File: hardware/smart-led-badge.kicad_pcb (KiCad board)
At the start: 4 copper layers, 118 x 76 mm, 1236 parts, among them J301 TYPE-C-31-M-12, J302 Battery JST-PH 2P, J501 SWD 2x5 1.27mm, Q201 AO3401A, Q202 AO3400A, Q203 AO3401A, Q204 AO3400A, Q301 AO3400A, Q302 AO3400A, Q303 AO3400A, Q701 AO3401A, Q702 AO3401A, Q703 AO3401A, Q704 AO3401A, Q705 AO3401A, Q706 AO3401A, Q707 AO3401A, Q708 AO3401A, Q709 AO3401A, Q710 AO3401A, Q711 AO3401A, Q712 AO3401A, Q713 AO3401A, Q714 AO3401A, Q715 AO3401A, Q716 AO3401A, Q717 AO3401A, Q718 AO3401A, Q719 AO3401A, Q720 AO3401A, Q721 AO3401A, Q722 AO3401A, Q723 AO3401A, Q724 AO3401A, Q725 AO3401A, Q726 AO3401A, Q727 AO3401A, Q728 AO3401A, Q729 AO3401A, Q730 AO3401A, Q731 AO3401A, Q732 AO3401A, SW1201 Mode/Next, SW1202 Action/Select, SW201 PCM12SMTR, U1101 NT3H2111W0FHKH, U201 TPS63802, U202 TPS61023, U301 TPD4E05U06, U302 BQ25620, U401 E73-2G4M08S1C, U601 TLC59283, U602 TLC59283, U701 SN74LVC8T245, U702 SN74HC595, U703 SN74HC595, U704 SN74HC595, U705 SN74HC595, U706 SN74LVC1G123, U707 SN74LVC1G04, U708 SN74LVC1G32, U901 ICM-42688-P, Y401 32.768kHz 9pF

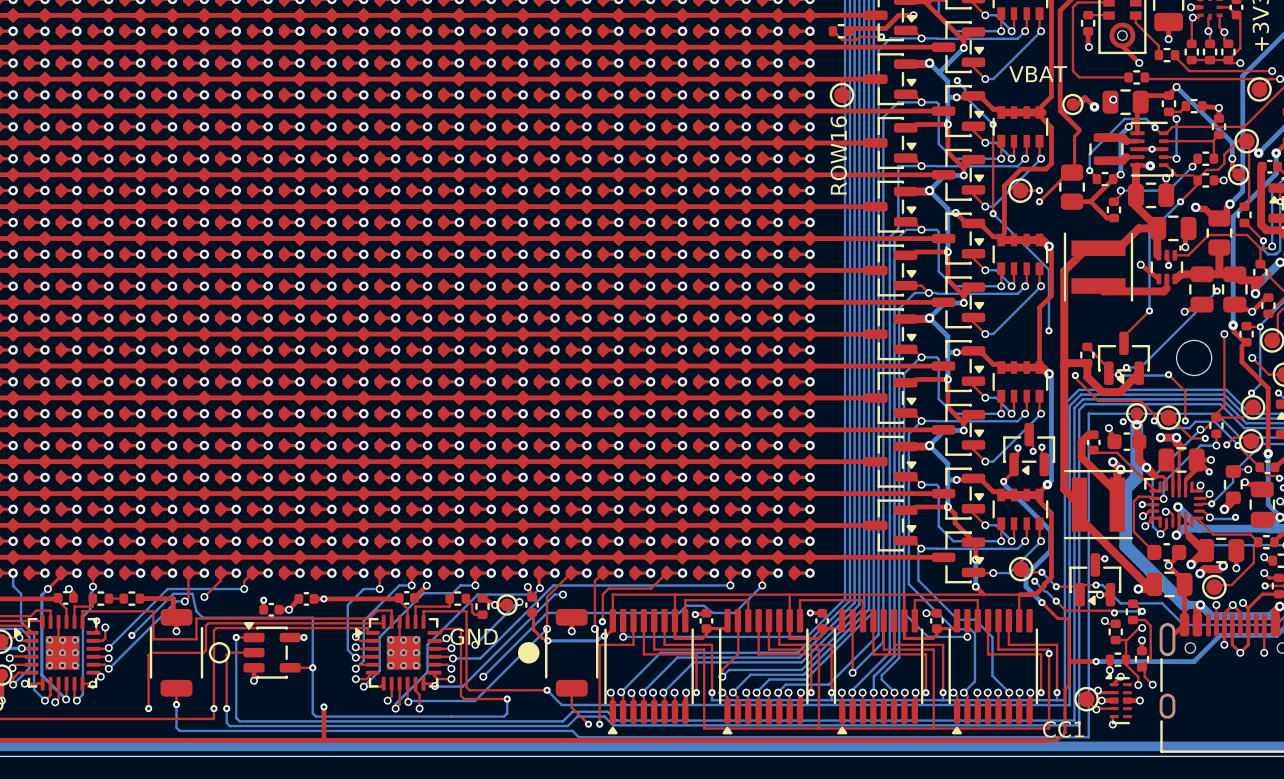
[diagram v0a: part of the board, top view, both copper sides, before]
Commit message: hw: move three vias out of component pads
The drill holes of the vias at C202.2, U201.8 and U601.13 reached into
the pads. Solder can wick down an open hole during reflow and starve the
joint, most of all on the two 0.25 mm-wide IC pins. Move the vias clear
of the pads, shifting the MODE_3V3 via and an In2 SYS segment to make
room, and refill the In1 GND plane.
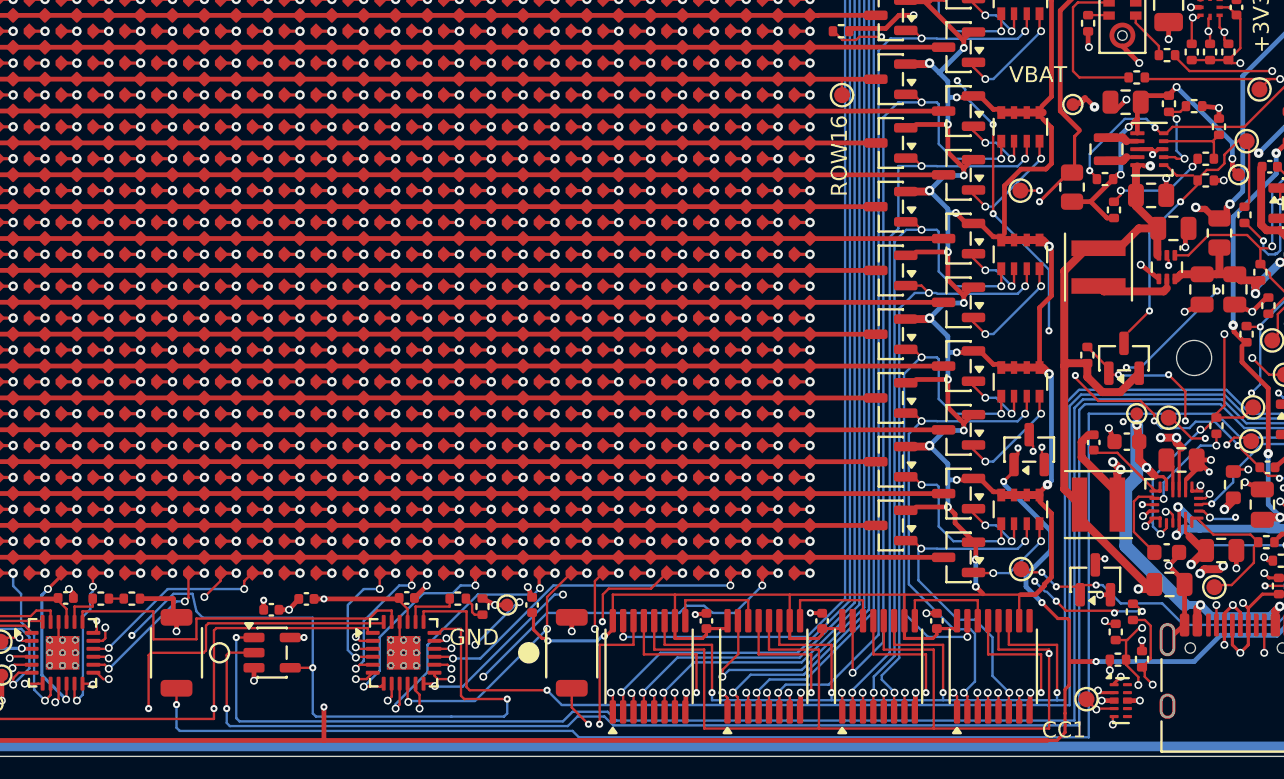
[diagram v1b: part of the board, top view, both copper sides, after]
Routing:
- net COL11: track 104.9 -> 106.0 mm
- net GND: track 108.8 -> 109.7 mm
- net /Regulators and Power Tree/MODE_3V3: track 5.19 -> 5.90 mm
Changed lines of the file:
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@@
 	)
 	(segment
+		(start 136.992185 88.239077)
+		(end 136.992185 87.952185)
+		(width 0.25)
+		(layer "F.Cu")
+		(net "GND")
+	)
+	(segment
 		(start 139 115.21)
 		(end 139 117.755)
@@
 	)
 	(segment
+		(start 136.94 87.9)
+		(end 136.24 87.9)
+		(width 0.25)
+		(layer "F.Cu")
+		(net "GND")
+	)
+	(segment
 		(start 134.5825 122.5)
 		(end 133.8 122.5)
@@
 	)
 	(segment
+		(start 134.679999 85.46)
+		(end 135.35 84.789999)
+		(width 0.3)
+		(layer "F.Cu")
+		(net "GND")
+	)
+	(segment
 		(start 143.88 109.25)
 		(end 142.785448 108.796621)
@@
 	)
 	(segment
+		(start 134.529999 85.46)
+		(end 134.679999 85.46)
+		(width 0.3)
+		(layer "F.Cu")
+		(net "GND")
+	)
+	(segment
 		(start 138.655 113.37)
 		(end 138 114.025)
@@
 	)
 	(segment
+		(start 136.992185 88.239077)
+		(end 137.331262 87.9)
+		(width 0.25)
+		(layer "F.Cu")
+		(net "GND")
+	)
+	(segment
 		(start 163.3 92.625)
 		(end 163.3 92.15)
@@
 	)
 	(segment
+		(start 137.331262 87.9)
+		(end 137.69 87.9)
+		(width 0.25)
+		(layer "F.Cu")
+		(net "GND")
+	)
+	(segment
 		(start 140.11 85.2)
 		(end 141.16 85.31)
@@
 	)
 	(segment
-		(start 134.529999 85.46)
-		(end 134.529999 84.789999)
-		(width 0.3)
+		(start 136.992185 87.952185)
+		(end 136.94 87.9)
+		(width 0.25)
 		(layer "F.Cu")
 		(net "GND")
@@
 	)
 	(segment
-		(start 136.24 87.9)
-		(end 136.965 87.9)
-		(width 0.25)
-		(layer "F.Cu")
-		(net "GND")
-	)
-	(segment
 		(start 118.135 80.325)
 		(end 120.254448 80.325)
@@
 	)
 	(segment
-		(start 137.69 87.9)
-		(end 136.965 87.9)
-		(width 0.25)
-		(layer "F.Cu")
-		(net "GND")
-	)
-	(segment
 		(start 155.12 103.96)
 		(end 155.1 103.4)
@@
 	)
 	(via
-		(at 136.965 87.9)
+		(at 136.992185 88.239077)
 		(size 0.45)
 		(drill 0.2)
@@
 	)
 	(via
-		(at 134.529999 84.789999)
+		(at 135.35 84.789999)
 		(size 0.5)
 		(drill 0.3)
@@
 	)
 	(segment
-		(start 143.4 87.9)
-		(end 143.65 88.15)
+		(start 136.85 88.95)
+		(end 137.55 88.95)
+		(width 0.3)
+		(layer "In2.Cu")
+		(net "SYS")
+	)
+	(segment
+		(start 138.6 87.9)
+		(end 143.4 87.9)
 		(width 0.3)
 		(layer "In2.Cu")
@@
 	)
 	(segment
-		(start 136.85 88.95)
-		(end 137.9 87.9)
+		(start 162 84.9)
+		(end 162 86.4)
 		(width 0.3)
 		(layer "In2.Cu")
@@
 	)
 	(segment
-		(start 137.9 87.9)
-		(end 143.4 87.9)
-		(width 0.3)
+		(start 151.35 106.85)
+		(end 155.25 106.85)
+		(width 0.15)
 		(layer "In2.Cu")
 		(net "SYS")
 	)
 	(segment
-		(start 162 84.9)
-		(end 162 86.4)
+		(start 143.4 87.9)
+		(end 143.65 88.15)
 		(width 0.3)
 		(layer "In2.Cu")
@@
 	)
 	(segment
-		(start 151.35 106.85)
-		(end 155.25 106.85)
-		(width 0.15)
+		(start 137.55 88.95)
+		(end 138.6 87.9)
+		(width 0.3)
 		(layer "In2.Cu")
 		(net "SYS")
@@
 	)
 	(segment
+		(start 71.150003 121.150003)
+		(end 70.75 120.75)
+		(width 0.15)
+		(layer "F.Cu")
+		(net "COL11")
+	)
+	(segment
 		(start 74.505025 112.494975)
 		(end 75.5 112.5)
@@
 	)
 	(segment
-		(start 70.75 120.75)
-		(end 70.5375 120.75)
-		(width 0.15)
-		(layer "F.Cu")
-		(net "COL11")
-	)
-	(segment
 		(start 74.505025 70.494975)
 		(end 75.5 70.5)
@@
 	)
 	(segment
+		(start 71.5 121.150003)
+		(end 71.150003 121.150003)
+		(width 0.15)
+		(layer "F.Cu")
+		(net "COL11")
+	)
+	(segment
 		(start 74.505025 58.494975)
 		(end 75.5 58.5)
@@
 	)
 	(segment
-		(start 71 121)
-		(end 70.75 120.75)
+		(start 70.75 120.75)
+		(end 70.5375 120.75)
 		(width 0.15)
 		(layer "F.Cu")
@@
 	)
 	(via
-		(at 71 121)
+		(at 71.5 121.150003)
 		(size 0.5)
 		(drill 0.3)
@@
 	)
 	(segment
-		(start 71 121)
-		(end 70.3 120.3)
-		(width 0.15)
-		(layer "In2.Cu")
-		(net "COL11")
-	)
-	(segment
 		(start 75.5 94.5)
 		(end 75.5 96.5)
@@
 	)
 	(segment
-		(start 74.975 115.025)
-		(end 75.5 114.5)
+		(start 72.399264 115.025)
+		(end 74.975 115.025)
 		(width 0.15)
 		(layer "In2.Cu")
@@
 	)
 	(segment
+		(start 71.150003 121.150003)
+		(end 70.3 120.3)
+		(width 0.15)
+		(layer "In2.Cu")
+		(net "COL11")
+	)
+	(segment
+		(start 70.3 117.124264)
+		(end 72.399264 115.025)
+		(width 0.15)
+		(layer "In2.Cu")
+		(net "COL11")
+	)
+	(segment
 		(start 75.5 62.5)
 		(end 75.5 64.5)
@@
 	)
 	(segment
+		(start 71.5 121.150003)
+		(end 71.150003 121.150003)
+		(width 0.15)
+		(layer "In2.Cu")
+		(net "COL11")
+	)
+	(segment
 		(start 75.5 78.5)
 		(end 75.5 80.5)
@@
 	)
 	(segment
-		(start 70.3 120.3)
-		(end 70.3 117.124264)
-		(width 0.15)
-		(layer "In2.Cu")
-		(net "COL11")
-	)
-	(segment
 		(start 75.5 72.5)
 		(end 75.5 74.5)
@@
 	)
 	(segment
-		(start 72.399264 115.025)
-		(end 74.975 115.025)
-		(width 0.15)
-		(layer "In2.Cu")
-		(net "COL11")
-	)
-	(segment
 		(start 75.5 80.5)
 		(end 75.5 82.5)
@@
 	)
 	(segment
+		(start 70.3 120.3)
+		(end 70.3 117.124264)
+		(width 0.15)
+		(layer "In2.Cu")
+		(net "COL11")
+	)
+	(segment
 		(start 75.5 110.5)
 		(end 75.5 112.5)
@@
 	)
 	(segment
-		(start 75.5 52.5)
-		(end 75.5 54.5)
-		(width 0.2)
-		(locked yes)
+		(start 74.975 115.025)
+		(end 75.5 114.5)
+		(width 0.15)
 		(layer "In2.Cu")
 		(net "COL11")
 	)
 	(segment
-		(start 70.3 117.124264)
-		(end 72.399264 115.025)
-		(width 0.15)
+		(start 75.5 52.5)
+		(end 75.5 54.5)
+		(width 0.2)
+		(locked yes)
 		(layer "In2.Cu")
 		(net "COL11")
@@
 	)
 	(segment
-		(start 138.4 88.4)
-		(end 138.5 88.5)
+		(start 138.73 85.56)
+		(end 139.09 85.2)
 		(width 0.15)
 		(layer "F.Cu")
@@
 	)
 	(segment
-		(start 137.69 88.4)
-		(end 138.4 88.4)
+		(start 138.019999 85.56)
+		(end 138.73 85.56)
 		(width 0.15)
 		(layer "F.Cu")
@@
 	)
 	(segment
-		(start 138.73 85.56)
-		(end 139.09 85.2)
+		(start 139 88.5)
+		(end 138.5 88.5)
 		(width 0.15)
 		(layer "F.Cu")
@@
 	)
 	(segment
-		(start 138.019999 85.56)
-		(end 138.73 85.56)
+		(start 138.4 88.4)
+		(end 137.69 88.4)
+		(width 0.15)
+		(layer "F.Cu")
+		(net "/Regulators and Power Tree/MODE_3V3")
+	)
+	(segment
+		(start 138.5 88.5)
+		(end 138.4 88.4)
 		(width 0.15)
 		(layer "F.Cu")
@@
 	)
 	(via
-		(at 138.5 88.5)
+		(at 139 88.5)
 		(size 0.5)
 		(drill 0.3)
@@
 	)
 	(segment
-		(start 138.5 88.5)
+		(start 138.5 88)
 		(end 138.5 86)
 		(width 0.15)
 		(layer "B.Cu")
+		(net "/Regulators and Power Tree/MODE_3V3")
+	)
+	(segment
+		(start 139 88.5)
+		(end 138.5 88)
+		(width 0.15)
+		(layer "B.Cu")
